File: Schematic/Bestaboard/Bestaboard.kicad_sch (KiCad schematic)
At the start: 12 parts, among them J1 S5B-XH-A, J2 S5B-XH-A, J3 S5B-XH-A, J4 S5B-XH-A, J5 QT02ASF83H0000G, J6 QT02ASF83H0000G, J7 S3B-XH-A, J8 S3B-XH-A, U6 DRV5032AJLPGM, U7 DRV5032AJLPGM

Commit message: Moved local copy schematic into repo.
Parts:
- removed J4: S5B-XH-A, Connector_JST:JST_XH_S5B-XH-A_1x05_P2.50mm_Horizontal, symbol Connector_Generic:Conn_01x05
- removed R1, R5: 10K, Resistor_SMD:R_0805_2012Metric_Pad1.20x1.40mm_HandSolder, symbol Device:R_Small_US
- added C10, C9: 1uF, Capacitor_SMD:C_0603_1608Metric_Pad1.08x0.95mm_HandSolder, symbol Device:C_US
- added H1, H2, H3, H4: MountingHole, MountingHole:MountingHole_3.2mm_M3_ISO14580, symbol Mechanical:MountingHole
- added J9: PRPC005SGAN-M71RC, Connector_PinHeader_2.54mm:PinHeader_1x05_P2.54mm_Vertical, symbol Connector:Conn_01x05_Pin
- J3: value S5B-XH-A -> PPTC051LGBN-RC; footprint Connector_JST:JST_XH_S5B-XH-A_1x05_P2.50mm_Horizontal -> Connector_PinHeader_2.54mm:PinHeader_1x05_P2.54mm_Horizontal; symbol Connector_Generic:Conn_01x05 -> Connector:Conn_01x05_Socket
- J5: value QT02ASF83H0000G -> PPTC061LGBN-RC; footprint TerminalBlock:TerminalBlock_MaiXu_MX126-5.0-02P_1x02_P5.00mm -> Connector_PinHeader_2.54mm:PinHeader_1x06_P2.54mm_Horizontal; symbol Connector:Screw_Terminal_01x02 -> Connector:Conn_01x06_Socket
- J6: value QT02ASF83H0000G -> PRPC006SGAN-M71RC; footprint TerminalBlock:TerminalBlock_MaiXu_MX126-5.0-02P_1x02_P5.00mm -> Connector_PinHeader_2.54mm:PinHeader_1x06_P2.54mm_Vertical; symbol Connector:Screw_Terminal_01x02 -> Connector:Conn_01x06_Pin
- J7, J8: footprint (none) -> Connector_JST:JST_XH_S3B-XH-A_1x03_P2.50mm_Horizontal
- U6, U7: value DRV5032AJLPGM -> DRV5032FALPGM
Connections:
- net LEFT_SERVO_4 is gone; now on net +5V: J1.5 (Pin_5)
- net RIGHT_SERVO_4 is gone; now on net +5V: J2.5 (Pin_5)
- net +5V: now also J5.2 (Pin_2), J5.3 (Pin_3), J6.2 (Pin_2), J6.3 (Pin_3), C10.1, C9.1; no longer J1.1 (Pin_1), J2.1 (Pin_1)
- net ALL_HOMED: now also J9.5 (Pin_5); no longer J3.5 (Pin_5)
- net GND: now also J5.4 (Pin_4), J5.5 (Pin_5), J5.6 (Pin_6), J6.4 (Pin_4), J6.5 (Pin_5), J6.6 (Pin_6), C10.2, C9.2; no longer J5.2 (Pin_2), J6.2 (Pin_2)
- net HOME: now also J9.4 (Pin_4)
- net RIGHT_OF_HOMED: now also J3.5 (Pin_5)
- net SHIFT: now also J9.2 (Pin_2)
- net STROBE: now also J9.3 (Pin_3)
- net DATA renamed DATA_OUT
- net Homing Logic/LEFT_HOMED renamed Homing Logic/LEFT_HOMED_n
- net Homing Logic/RIGHT_HOMED renamed Homing Logic/RIGHT_HOMED_n
- net LEFT_HOMED renamed LEFT_HOMED_n
- net LEFT_SERVO_1 renamed LEFT_STEPPER_3
- net LEFT_SERVO_2 renamed LEFT_STEPPER_2
- net LEFT_SERVO_3 renamed LEFT_STEPPER_1
- net RIGHT_HOMED renamed RIGHT_HOMED_n
- net RIGHT_SERVO_1 renamed RIGHT_STEPPER_3
- net RIGHT_SERVO_2 renamed RIGHT_STEPPER_2
- net RIGHT_SERVO_3 renamed RIGHT_STEPPER_1
- new net DATA_IN: J9.1 (Pin_1)
- new net LEFT_STEPPER_4: J1.1 (Pin_1)
- new net RIGHT_STEPPER_4: J2.1 (Pin_1)
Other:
- sheet Servo Control renamed Stepper Control
- sheet Homing Logic ports: added LEFT_HOMED_n, RIGHT_HOMED_n; removed LEFT_HOMED, RIGHT_HOMED
- sheet Stepper Control ports: added DATA_IN, DATA_OUT, LEFT_STEPPER_1, LEFT_STEPPER_2, LEFT_STEPPER_3, LEFT_STEPPER_4, RIGHT_STEPPER_1, RIGHT_STEPPER_2, RIGHT_STEPPER_3, RIGHT_STEPPER_4; removed DATA, LEFT_SERVO_1, LEFT_SERVO_2, LEFT_SERVO_3, LEFT_SERVO_4, RIGHT_SERVO_1, RIGHT_SERVO_2, RIGHT_SERVO_3, RIGHT_SERVO_4
- note added: "Bulk Decoupling, place at power connectors."
- note added: "LEFT HOMING SENSOR"
- note added: "LEFT POWER IN"
- note added: "LEFT SIGNALS"
- note added: "LEFT STEPPER"
- note added: "RIGHT HOMING SENSOR"
- note added: "RIGHT POWER OUT"
- note added: "RIGHT SIGNALS"
- note added: "RIGHT STEPPER"
- note removed: "ADD: LEDs Decouplllilng"
- moved on the sheet: J7

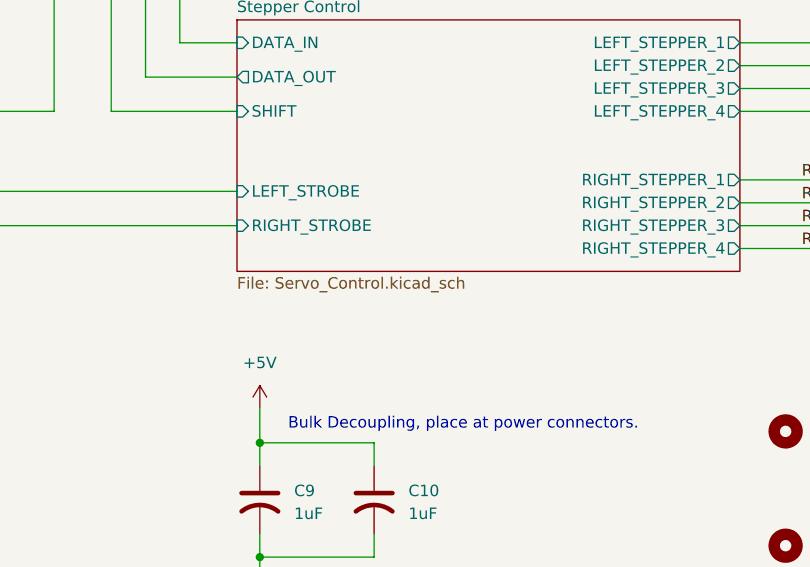
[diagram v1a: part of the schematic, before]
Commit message: Prints, Schematic, PCB, Code Update
Prints - Created print plates for flips, drum and frame, updated frame to have mounting holes on the bottom.
PCB/Schematic - Changed to 14 pin NAND chip, updated parameters.
Code - Changed code to alternate between homing and character rotation.
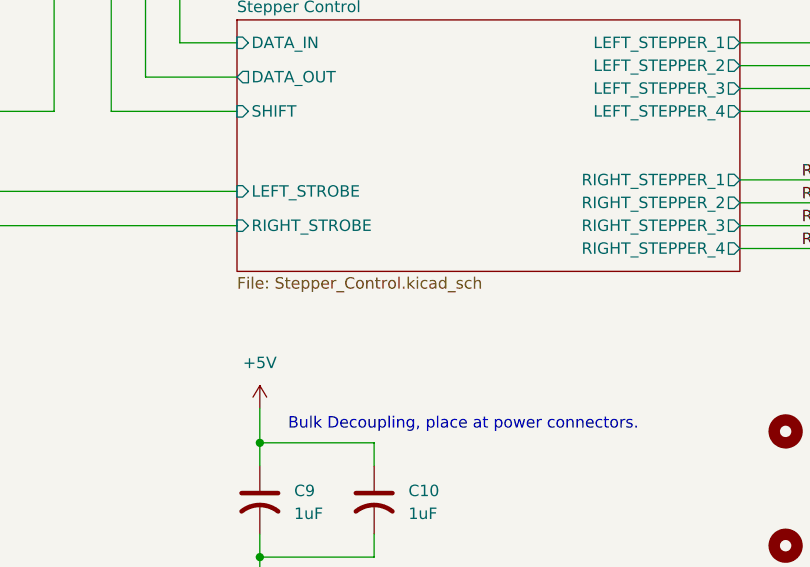
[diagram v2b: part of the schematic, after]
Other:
- sheet Stepper Control: file Servo_Control.kicad_sch -> Stepper_Control.kicad_sch
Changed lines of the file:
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@@
 			)
 		)
-		(property "Datasheet" "~"
+		(property "Datasheet" "https://www.jst-mfg.com/product/pdf/eng/eXH.pdf"
 			(at 254 92.71 0)
 			(effects
@@
 			)
 		)
-		(property "Datasheet" "~"
+		(property "Datasheet" "https://mm.digikey.com/Volume0/opasdata/d220001/medias/docus/937/Female_Headers.100_DS.pdf"
 			(at 39.37 43.18 0)
 			(effects
@@
 			)
 		)
-		(property "Datasheet" "~"
+		(property "Datasheet" "https://mm.digikey.com/Volume0/opasdata/d220001/medias/docus/937/Female_Headers.100_DS.pdf"
 			(at 39.37 24.13 0)
 			(effects
@@
 			)
 		)
-		(property "Datasheet" ""
+		(property "Datasheet" "https://www.ti.com/lit/ds/symlink/drv5032.pdf"
 			(at 52.07 165.1 0)
 			(effects
@@
 			)
 		)
-		(property "Datasheet" "~"
+		(property "Datasheet" "https://www.jst-mfg.com/product/pdf/eng/eXH.pdf"
 			(at 39.37 115.57 0)
 			(effects
@@
 			)
 		)
-		(property "Datasheet" "~"
+		(property "Datasheet" "https://mm.digikey.com/Volume0/opasdata/d220001/medias/docus/2610/x%20RxCxxxSxxN-M71RC_%2011637-B.pdf"
 			(at 254 24.13 0)
 			(effects
@@
 			)
 		)
-		(property "Datasheet" ""
+		(property "Datasheet" "https://www.ti.com/lit/ds/symlink/drv5032.pdf"
 			(at 105.41 163.83 0)
 			(effects
@@
 			)
 		)
-		(property "Datasheet" ""
+		(property "Datasheet" "https://yageogroup.com/content/datasheet/asset/file/KEM_C1002_X7R_SMD"
 			(at 184.15 140.97 0)
 			(effects
@@
 			)
 		)
-		(property "Datasheet" ""
+		(property "Datasheet" "https://yageogroup.com/content/datasheet/asset/file/KEM_C1002_X7R_SMD"
 			(at 171.45 140.97 0)
 			(effects
@@
 			)
 		)
-		(property "Datasheet" "~"
+		(property "Datasheet" "https://www.jst-mfg.com/product/pdf/eng/eXH.pdf"
 			(at 254 107.95 0)
 			(effects
@@
 			)
 		)
-		(property "Datasheet" "~"
+		(property "Datasheet" "https://www.jst-mfg.com/product/pdf/eng/eXH.pdf"
 			(at 39.37 101.6 0)
 			(effects
@@
 			)
 		)
-		(property "Datasheet" "~"
+		(property "Datasheet" "https://mm.digikey.com/Volume0/opasdata/d220001/medias/docus/2610/x%20RxCxxxSxxN-M71RC_%2011637-B.pdf"
 			(at 254 43.18 0)
 			(effects
@@
 			)
 		)
-		(property "Sheetfile" "Servo_Control.kicad_sch"
+		(property "Sheetfile" "Stepper_Control.kicad_sch"
 			(at 168.91 116.1546 0)
 			(effects

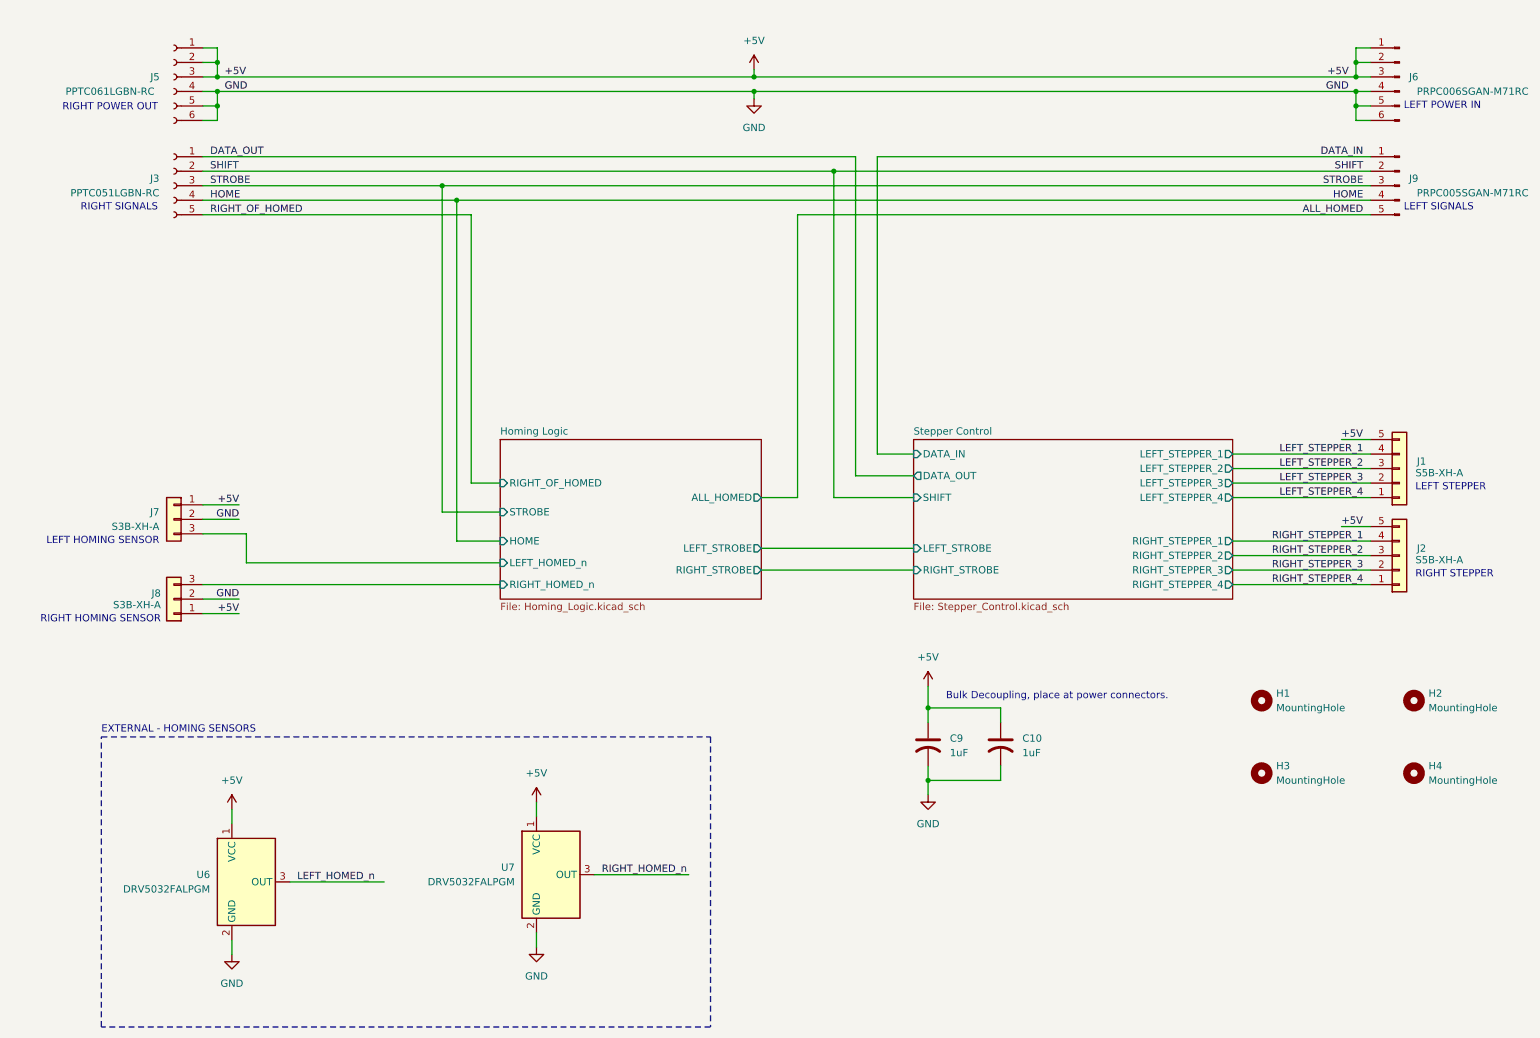
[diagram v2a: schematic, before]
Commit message: Output BOM and updated parts list
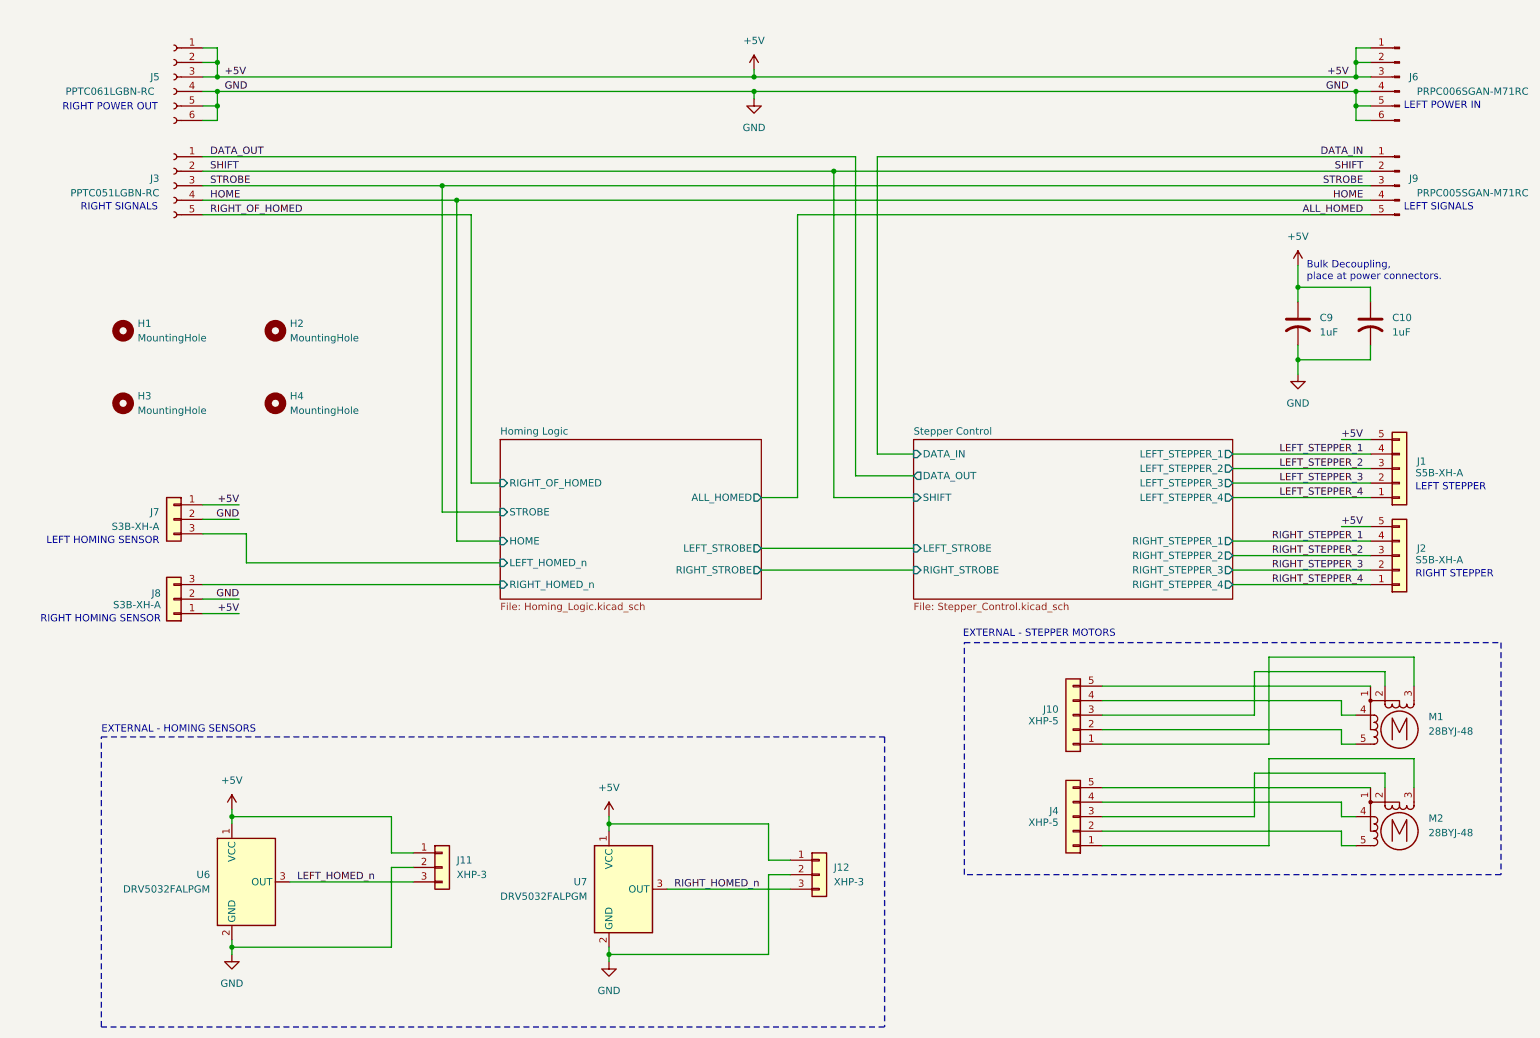
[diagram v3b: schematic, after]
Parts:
- added J10, J4: XHP-5, symbol Connector_Generic:Conn_01x05
- added J11, J12: XHP-3, symbol Connector_Generic:Conn_01x03
- added M1, M2: 28BYJ-48, symbol Motor:Stepper_Motor_unipolar_5pin
- C10, C9: Purchase Link (none) -> https://www.digikey.com/en/products/detail/kemet/C0603C105K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
- J1, J2, J7, J8: Purchase Link (none) -> https://www.digikey.com/en/products/detail/jst-sales-americ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
- J3, J5, J6, J9: Purchase Link (none) -> https://www.digikey.com/en/products/detail/sullins-connecto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
- U6, U7: Purchase Link (none) -> https://www.digikey.com/en/products/detail/texas-instrument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
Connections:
- net +5V: now also J11.1 (Pin_1), J12.1 (Pin_1)
- net GND: now also J11.2 (Pin_2), J12.2 (Pin_2)
- net LEFT_HOMED_n: now also J11.3 (Pin_3)
- net RIGHT_HOMED_n: now also J12.3 (Pin_3)
- new net: J4.5 (Pin_5), M2.1
- new net: J4.3 (Pin_3), M2.2
- new net: J4.1 (Pin_1), M2.3 (-)
- new net: J4.4 (Pin_4), M2.4
- new net: J4.2 (Pin_2), M2.5
- new net: J10.5 (Pin_5), M1.1
- new net: J10.3 (Pin_3), M1.2
- new net: J10.1 (Pin_1), M1.3 (-)
- new net: J10.4 (Pin_4), M1.4
- new net: J10.2 (Pin_2), M1.5
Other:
- note added: "EXTERNAL - STEPPER MOTORS"
- moved on the sheet: C10, C9, H1, H2, H3, H4, U7

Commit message: Schematic PDF & Schematic
Updated title block to include date and name. Created PDF of scheamtic.
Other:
- company: (none) -> Isaac Rasmusson
- title: (none) -> Bestaboard
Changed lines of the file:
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@@
 	(generator_version "9.0")
 	(paper "A4")
+	(title_block
+		(title "Bestaboard")
+		(date "2026-05-21")
+		(rev "A")
+		(company "Isaac Rasmusson")
+	)
 	(rectangle
 		(start 177.8 123.19)
